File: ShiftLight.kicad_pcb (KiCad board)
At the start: 2 copper layers, 63 x 12 mm, 11 parts, among them U1 MSPM0C1104SDDFR, U2 LMR544xx, U3 KTD2052A/B

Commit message: Layout: Import, start placement
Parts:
- added C1: 100n, Capacitor_SMD:C_0805_2012Metric, F.Cu at (109.1, 112.6)
- added C10: 100n, Capacitor_SMD:C_0402_1005Metric, F.Cu at (162.9, 89.8)
- added C11: 10u, Capacitor_SMD:C_1206_3216Metric, F.Cu at (97.6, 110.9)
- added C12: 100n, Capacitor_SMD:C_0402_1005Metric, F.Cu at (162.9, 87.3)
- added C13: 100n, Capacitor_SMD:C_0402_1005Metric, F.Cu at (162.9, 92.3)
- added C2: 100n, Capacitor_SMD:C_0805_2012Metric, F.Cu at (109.1, 109.5)
- added C3: 10n, Capacitor_SMD:C_0402_1005Metric, F.Cu at (94.7, 88.7)
- added C4: 10n, Capacitor_SMD:C_0402_1005Metric, F.Cu at (92.9, 88.1)
- added C5: 100n, Capacitor_SMD:C_0603_1608Metric, F.Cu at (188.9, 79.3)
- added C6: 4.7u, Capacitor_SMD:C_1206_3216Metric, F.Cu at (108.4, 100.3)
- added C7: 100n, Capacitor_SMD:C_0603_1608Metric, F.Cu at (188.9, 81.8)
- added C8: 100n, Capacitor_SMD:C_0402_1005Metric, F.Cu at (137.4, 105.3)
- added C9: 10u, Capacitor_SMD:C_1206_3216Metric, F.Cu at (114.8, 108.9)
- added D10: XLMDK12D, LED_THT:LED_D5.0mm_IRGrey, F.Cu at (133.6, 83.8)
- added D11: XLMDK12D, LED_THT:LED_D5.0mm_IRGrey, F.Cu at (126.3, 83.8)
- added D12: ESDA5V3SC5, Package_TO_SOT_SMD:SOT-23-5, F.Cu at (127.5, 89.2)
- added D9: XLMYK12D, LED_THT:LED_D5.0mm_IRGrey, F.Cu at (119.0, 83.8)
- added F1: F0603G0R15FNTR, Fuse:Fuse_0603_1608Metric, F.Cu at (97.6, 88.1)
- added FB1: BLM15PX601SZ1D, Inductor_SMD:L_0402_1005Metric, F.Cu at (137.4, 103.3)
- added J1: 0533980471, Connector_Molex:Molex_PicoBlade_53398-0471_1x04-1MP_P1.25mm_Vertical, B.Cu at (94.7, 87.3)
- added J2: 0533980571, Connector_Molex:Molex_PicoBlade_53398-0571_1x05-1MP_P1.25mm_Vertical, B.Cu at (126.7, 87.3)
- added JP1: ~, Jumper:SolderJumper-2_P1.3mm_Bridged_RoundedPad1.0x1.5mm, F.Cu at (104.7, 113.4)
- added L1: 15u, Inductor_SMD:L_TDK_VLS3015CX, F.Cu at (112.9, 114.3)
- added R1: 5k6, Resistor_SMD:R_0402_1005Metric, F.Cu at (117.0, 99.9)
- added R10: 68R, Resistor_SMD:R_0402_1005Metric, F.Cu at (96.1, 97.9)
- added R11: 68R, Resistor_SMD:R_0402_1005Metric, F.Cu at (96.1, 99.9)
- added R12: 68R, Resistor_SMD:R_0402_1005Metric, F.Cu at (96.1, 101.9)
- added R13: 68R, Resistor_SMD:R_0402_1005Metric, F.Cu at (99.0, 97.9)
- added R14: 68R, Resistor_SMD:R_0402_1005Metric, F.Cu at (99.0, 99.9)
- added R15: 68R, Resistor_SMD:R_0402_1005Metric, F.Cu at (99.0, 101.9)
- added R2: 1k8, Resistor_SMD:R_0402_1005Metric, F.Cu at (93.0, 89.5)
- added R3: 100k, Resistor_SMD:R_0402_1005Metric, F.Cu at (188.9, 84.4)
- added R4: 32k, Resistor_SMD:R_0402_1005Metric, F.Cu at (188.9, 86.9)
- added R5: 3k3, Resistor_SMD:R_0402_1005Metric, F.Cu at (162.9, 94.9)
- added R6: 3k3, Resistor_SMD:R_0402_1005Metric, F.Cu at (162.9, 97.4)
- added R7: 68R, Resistor_SMD:R_0402_1005Metric, F.Cu at (93.2, 99.9)
- added R8: 68R, Resistor_SMD:R_0402_1005Metric, F.Cu at (93.2, 101.9)
- added R9: 5k6, Resistor_SMD:R_0402_1005Metric, F.Cu at (93.2, 97.9)
- added TP1: ~, TestPoint:TestPoint_Pad_D1.0mm, F.Cu at (119.1, 108.5)
- added TP2: ~, TestPoint:TestPoint_Pad_D1.0mm, F.Cu at (134.5, 103.9)
- added TP3: ~, TestPoint:TestPoint_Pad_D1.0mm, F.Cu at (134.5, 106.9)
- added TP4: ~, TestPoint:TestPoint_Pad_D1.0mm, F.Cu at (119.1, 105.4)
- added TP5: ~, TestPoint:TestPoint_Pad_D1.0mm, F.Cu at (72.9, 74.9)
- added TP6: ~, TestPoint:TestPoint_Pad_D1.0mm, F.Cu at (93.3, 110.8)
- added U4: TLC59208F, Package_DFN_QFN:Texas_RGY_R-PVQFN-N16_EP2.05x2.55mm_ThermalVias, B.Cu at (109.0, 87.9)
- added U5: VEML7700, Sensor:Vishay_VEML7700, F.Cu at (90.0, 78.6)
- added U6: TLV803E, Package_TO_SOT_SMD:SOT-323_SC-70, F.Cu at (94.0, 117.4)
- D1: value LD271 -> PMEG6010ER; footprint LED_THT:LED_D5.0mm_IRGrey -> Diode_SMD:Nexperia_CFP3_SOD-123W; moved to B.Cu
- D2: value LD271 -> SMAJ30CA; footprint LED_THT:LED_D5.0mm_IRGrey -> Diode_SMD:D_SMA
- D3: value LD271 -> VESD05B1-02V; footprint LED_THT:LED_D5.0mm_IRGrey -> Diode_SMD:D_SOD-523
- D4, D5, D6: value LD271 -> XLVG12D
- D7, D8: value LD271 -> XLMYK12D
- U1: value MSPM0C1104SDDFR -> VOS618A; footprint Package_TO_SOT_SMD:SOT-23-8 -> Package_SO:SSOP-4_4.4x2.6mm_P1.27mm
- U2: value LMR544xx -> LMR51406YDBV
- U3: value KTD2052A/B -> MSPM0C1104SDDFR; footprint Package_DFN_QFN:DFN-8-1EP_2x2mm_P0.5mm_EP0.9x1.5mm -> Package_TO_SOT_SMD:SOT-23-8
- moved U1 60.5 mm to (85.9, 88.9), turned to 180 degrees
- moved D4 40.7 mm to (82.5, 83.8)
- moved U3 34.8 mm to (167.4, 93.1)
- moved D6 34.4 mm to (97.1, 83.8), turned to 0 degrees
- moved D8 27.6 mm to (111.7, 83.8), turned to 0 degrees
- moved D2 18.0 mm to (102.8, 89.2), turned to 180 degrees
- moved D1 16.6 mm to (102.1, 84.7), turned to -90 degrees
- moved D5 13.2 mm to (89.8, 83.8)
- moved D3 12.1 mm to (90.9, 88.8)
- moved U2 11.7 mm to (150.1, 79.5)
- moved D7 8.47 mm to (104.4, 83.8)
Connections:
- net 12V0 renamed Net-(JP1-B)
- D1 pad 1: unconnected-(D1-K-Pad1) -> 12V_IN
- D1 pad 2: unconnected-(D1-A-Pad2) -> Net-(D1-A)
- D2 pad 1: unconnected-(D2-K-Pad1) -> GND
- D2 pad 2: unconnected-(D2-A-Pad2) -> Net-(D1-A)
- D3 pad 1: unconnected-(D3-K-Pad1) -> Net-(D3-K)
- D3 pad 2: unconnected-(D3-A-Pad2) -> Net-(D3-A)
- D4 pad 1: unconnected-(D4-K-Pad1) -> Net-(D4-K)
- D4 pad 2: unconnected-(D4-A-Pad2) -> Net-(D4-A)
- D5 pad 1: unconnected-(D5-K-Pad1) -> Net-(D5-K)
- D5 pad 2: unconnected-(D5-A-Pad2) -> Net-(D5-A)
- D6 pad 1: unconnected-(D6-K-Pad1) -> Net-(D6-K)
- D6 pad 2: unconnected-(D6-A-Pad2) -> Net-(D6-A)
- D7 pad 1: unconnected-(D7-K-Pad1) -> Net-(D7-K)
- D7 pad 2: unconnected-(D7-A-Pad2) -> Net-(D7-A)
- D8 pad 1: unconnected-(D8-K-Pad1) -> Net-(D8-K)
- D8 pad 2: unconnected-(D8-A-Pad2) -> Net-(D8-A)
- U1 pad 1: unconnected-(U1-PA27/A0-Pad1) -> Net-(D3-K)
- U1 pad 2: unconnected-(U1-PA1/NRST-Pad2) -> Net-(D3-A)
- U1 pad 4: 3V3 -> /01_Input/TACHO
- U3 pad 1: unconnected-(U3-SCL-Pad1) -> /01_Input/TACHO
- U3 pad 2: unconnected-(U3-SDA-Pad2) -> /02_MCU/I2C_SCL
- U3 pad 3: unconnected-(U3-LED4-Pad3) -> GND
- U3 pad 4: unconnected-(U3-LED3-Pad4) -> 3V3
- U3 pad 5: unconnected-(U3-LED2-Pad5) -> /02_MCU/I2C_SDA
- U3 pad 6: unconnected-(U3-LED1-Pad6) -> /02_MCU/SWDIO
- U3 pad 7: GND -> /02_MCU/SWCLK
- U3 pad 8: 3V3 -> Net-(U3-PA24/A3)
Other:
- board size 63 x 12 mm -> 66.3 x 15.2 mm

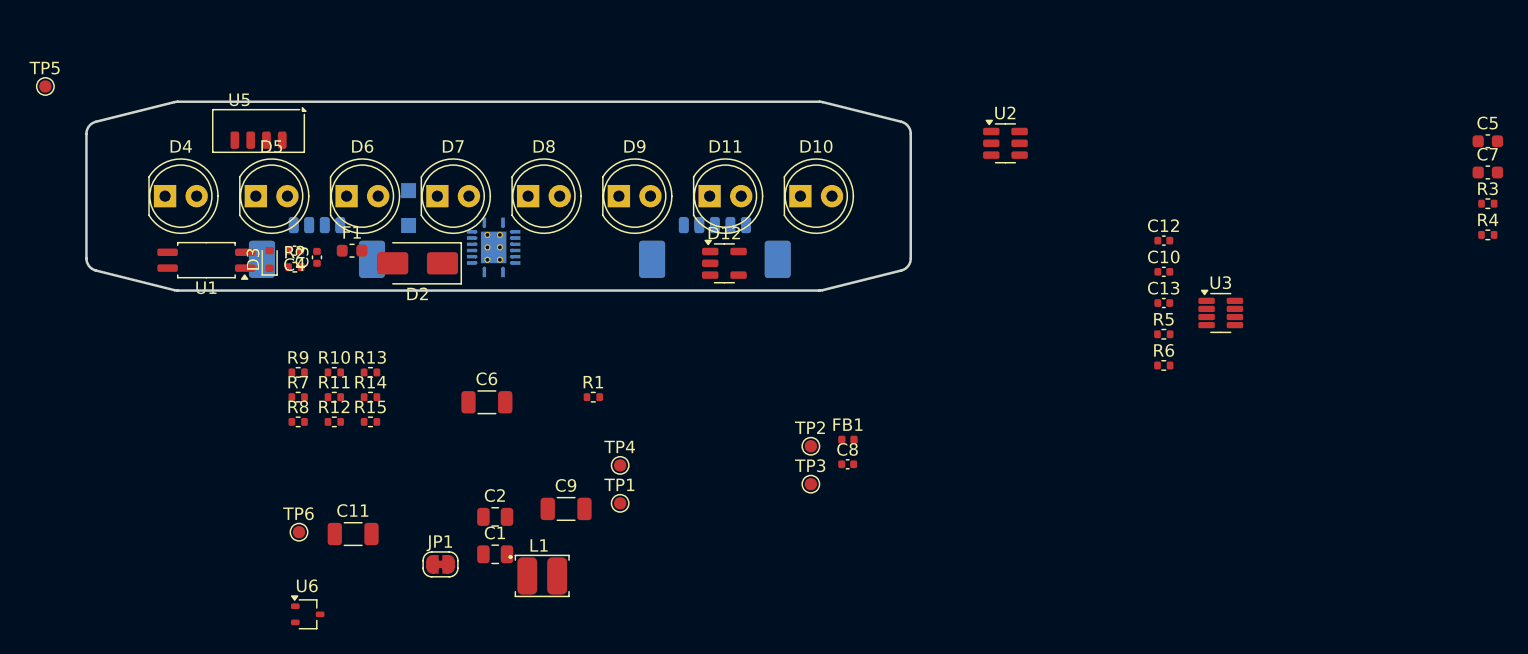
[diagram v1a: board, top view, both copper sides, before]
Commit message: Layout: Initial component placement
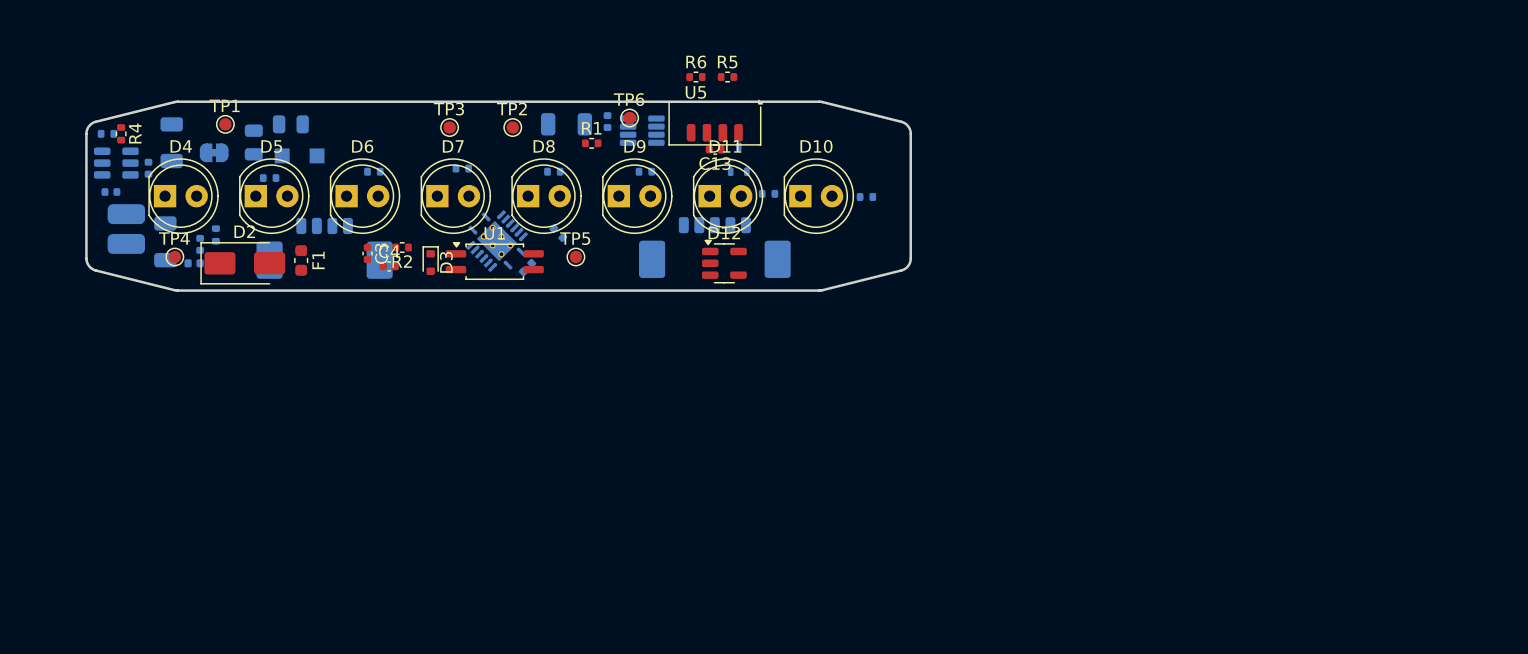
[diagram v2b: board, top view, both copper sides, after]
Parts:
- C1, C10, C11, C12, C2, C6, C8, C9, FB1, JP1, L1, R10, R11, R12, R13, R14, R15, R3, R7, R8, R9, U2, U3, U6: moved to B.Cu
- C5, C7: footprint Capacitor_SMD:C_0603_1608Metric -> Capacitor_SMD:C_0402_1005Metric; moved to B.Cu
- moved R3 111.2 mm to (77.9, 78.7), turned to 180 degrees
- moved C5 110.8 mm to (78.2, 83.4)
- moved R4 110.2 mm to (79.0, 78.7), turned to -90 degrees
- moved C7 107.7 mm to (81.2, 81.5), turned to -90 degrees
- moved U2 71.5 mm to (78.6, 81.1)
- moved C8 55.0 mm to (85.3, 87.6), turned to 90 degrees
- moved FB1 54.5 mm to (84.9, 89.2)
- moved C10 51.2 mm to (111.7, 89.5), turned to -135 degrees
- moved U6 50.4 mm to (128.7, 80.8), turned to 90 degrees
- moved U3 48.8 mm to (120.9, 78.5)
- moved C12 45.8 mm to (118.1, 77.8), turned to -90 degrees
- moved TP5 44.8 mm to (115.6, 88.6)
- moved R6 44.2 mm to (125.2, 74.2)
- moved TP1 44.0 mm to (87.4, 78.0)
- moved L1 43.6 mm to (79.4, 86.4), turned to -90 degrees
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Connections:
- C3 pad 1: Net-(J1-Pin_3) -> Net-(J1-Pin_1)
- D12 pad 1: +3V3 -> /02_MCU/SWDIO
- D12 pad 3: /02_MCU/I2C_SCL -> /02_MCU/SWCLK
- D12 pad 4: /02_MCU/SWDIO -> +3V3
- D12 pad 5: /02_MCU/SWCLK -> /02_MCU/I2C_SCL
- F1 pad 1: Net-(J1-Pin_1) -> Net-(J1-Pin_4)
- J1 pad 2: GND -> Net-(D3-A)
- J1 pad 3: Net-(J1-Pin_3) -> GND
- J1 pad 4: Net-(D3-A) -> Net-(J1-Pin_4)
- R2 pad 2: Net-(J1-Pin_3) -> Net-(J1-Pin_1)

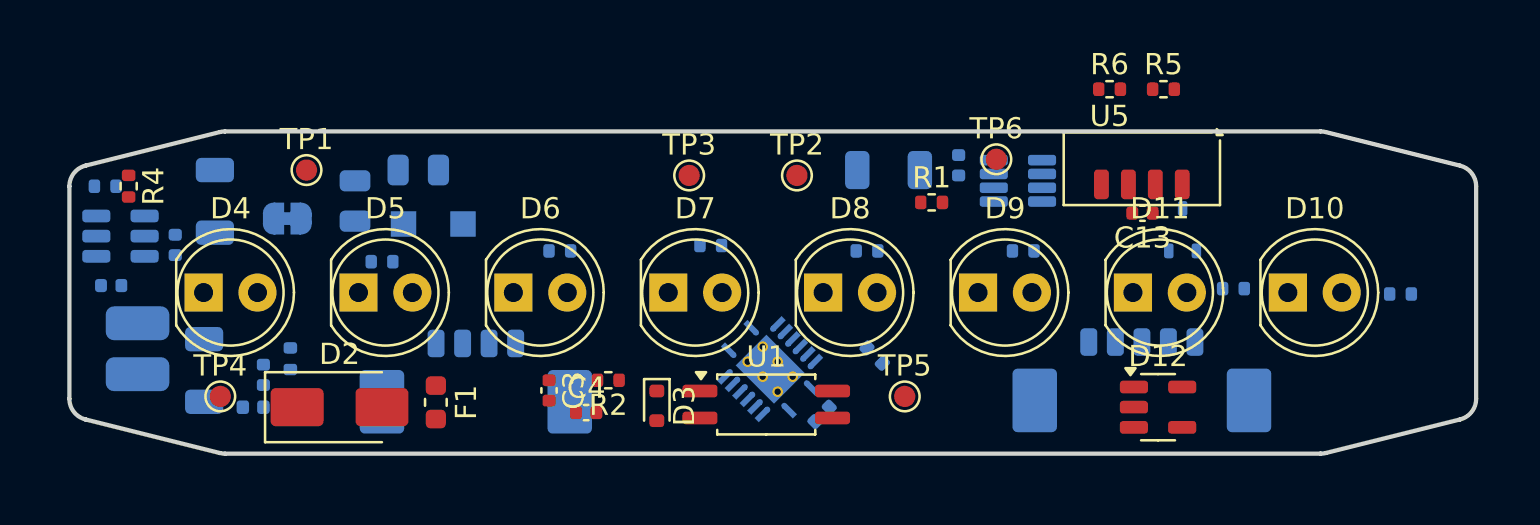
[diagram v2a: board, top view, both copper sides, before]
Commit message: Layout: Finish routing, start silkscreen cleanup
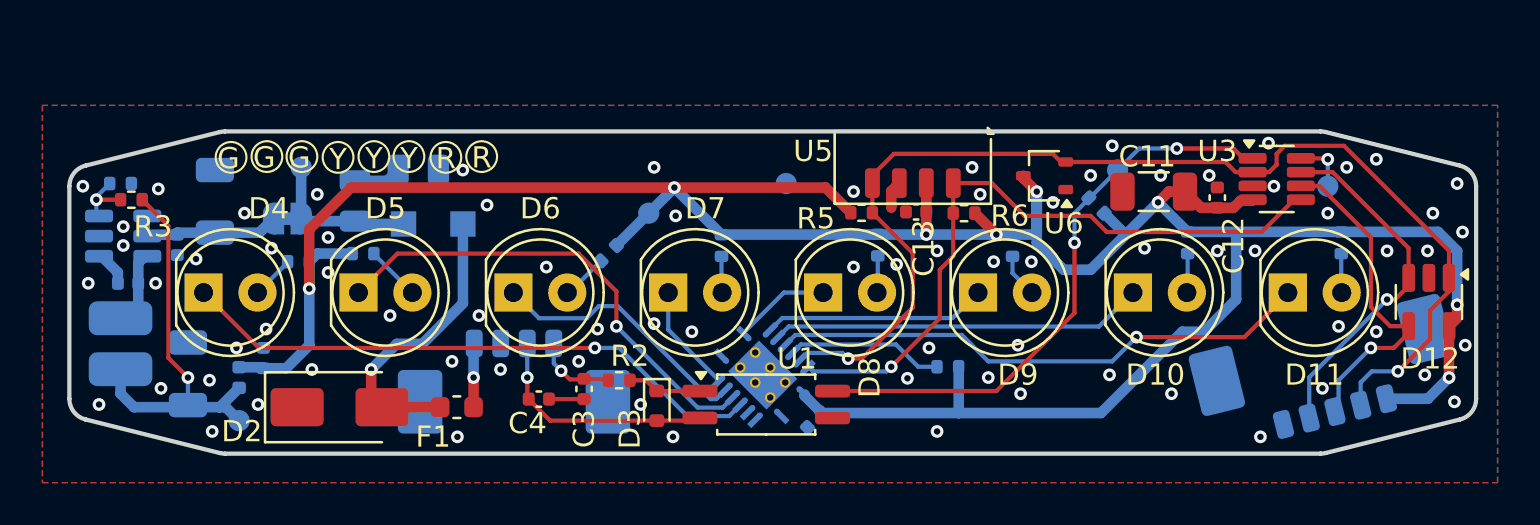
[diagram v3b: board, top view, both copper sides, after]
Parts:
- C11, C12, R3, U3, U6: moved to F.Cu
- R1, R4, TP1, TP2, TP3, TP4, TP5, TP6: moved to B.Cu
- moved TP6 15.7 mm to (135.5, 78.7), turned to 180 degrees
- moved R5 15.4 mm to (113.5, 80.0)
- moved TP5 14.6 mm to (125.6, 78.0), turned to 180 degrees
- moved D12 13.7 mm to (140.3, 84.2), turned to -90 degrees
- moved C11 12.5 mm to (127.3, 79.0)
- moved C12 12.3 mm to (130.3, 79.3), turned to 90 degrees
- moved U3 12.2 mm to (133.1, 78.4)
- moved U5 10.8 mm to (116.0, 77.9)
- moved C13 10.7 mm to (116.1, 79.9)
- moved R14 10.3 mm to (128.9, 81.4), turned to 90 degrees
- moved R6 9.01 mm to (118.4, 80.0), turned to 180 degrees
- moved J2 8.84 mm to (135.5, 88.1), turned to 14 degrees
- moved R1 7.77 mm to (124.6, 79.6), turned to 135 degrees
- moved D10 7.30 mm to (126.3, 83.8)
- moved D11 7.30 mm to (133.6, 83.8)
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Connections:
- D12 pad 1: /02_MCU/SWDIO -> /02_MCU/I2C_SCL
- D12 pad 4: +3V3 -> /02_MCU/SWDIO
- D12 pad 5: /02_MCU/I2C_SCL -> 3V3
- J2 pad 1: +3V3 -> GND
- J2 pad 2: /02_MCU/I2C_SCL -> /02_MCU/SWCLK
- J2 pad 4: /02_MCU/SWCLK -> /02_MCU/I2C_SCL
- J2 pad 5: GND -> 3V3
- U6 pad 3: +3V3 -> 3V3
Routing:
- net 3V3: track 0.00 -> 137.6 mm, vias 0 -> 8
- net /02_MCU/I2C_SCL: track 0.00 -> 53.8 mm, vias 0 -> 2
- net /02_MCU/I2C_SDA: track 0.00 -> 31.9 mm, vias 0 -> 1
- net Net-(D4-K): track 0.00 -> 27.9 mm, vias 0 -> 1
- net /01_Input/TACHO: track 0.00 -> 27.5 mm, vias 0 -> 2
- net Net-(D11-K): track 0.00 -> 25.7 mm, vias 0 -> 1
- net Net-(D5-K): track 0.00 -> 22.5 mm, vias 0 -> 1
- net Net-(C9-Pad2): track 0.00 -> 19.1 mm, vias 0 -> 1
- net Net-(D10-K): track 0.00 -> 17.6 mm
- net /02_MCU/SWCLK: track 0.00 -> 16.7 mm, vias 0 -> 1
- net /02_MCU/SWDIO: track 0.00 -> 15.8 mm, vias 0 -> 1
- net Net-(D1-A): track 0.00 -> 14.1 mm, vias 0 -> 1
- net Net-(D6-K): track 0.00 -> 12.7 mm
- net Net-(D3-A): track 0.00 -> 11.2 mm, vias 0 -> 1
- net Net-(D9-K): track 0.00 -> 10.5 mm
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- added copper zone on B.Cu, net GND
- added copper zone on F.Cu, net GND
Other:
- board text added: "G"
- board text added: "R"
- board text added: "Y"

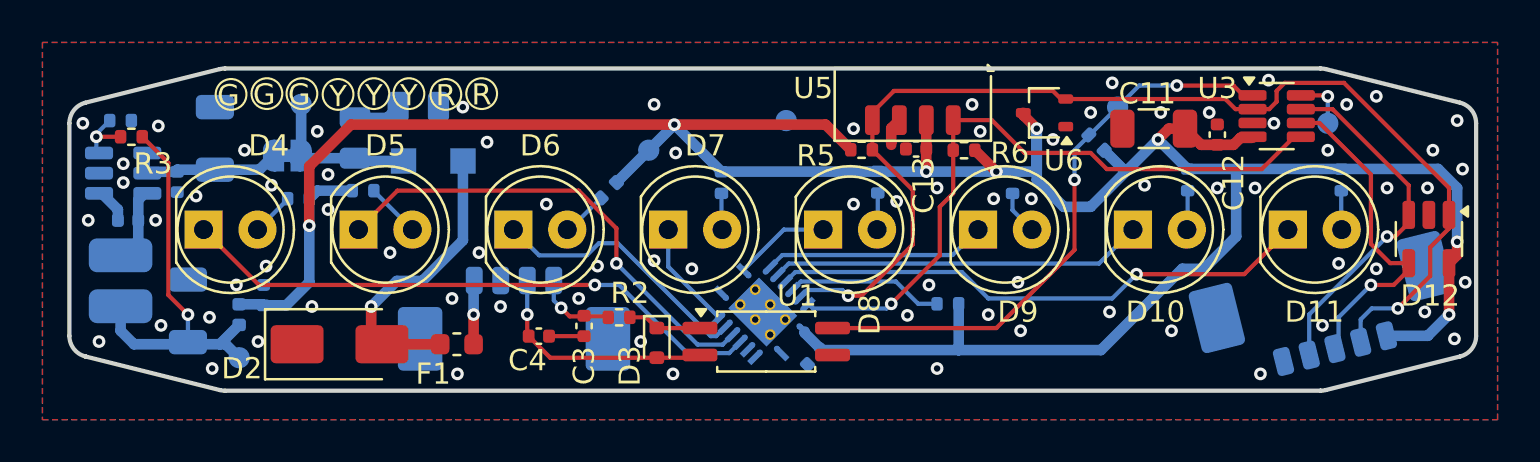
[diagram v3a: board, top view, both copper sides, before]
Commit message: Layout: Cleanup silkscreen and assembly drawing
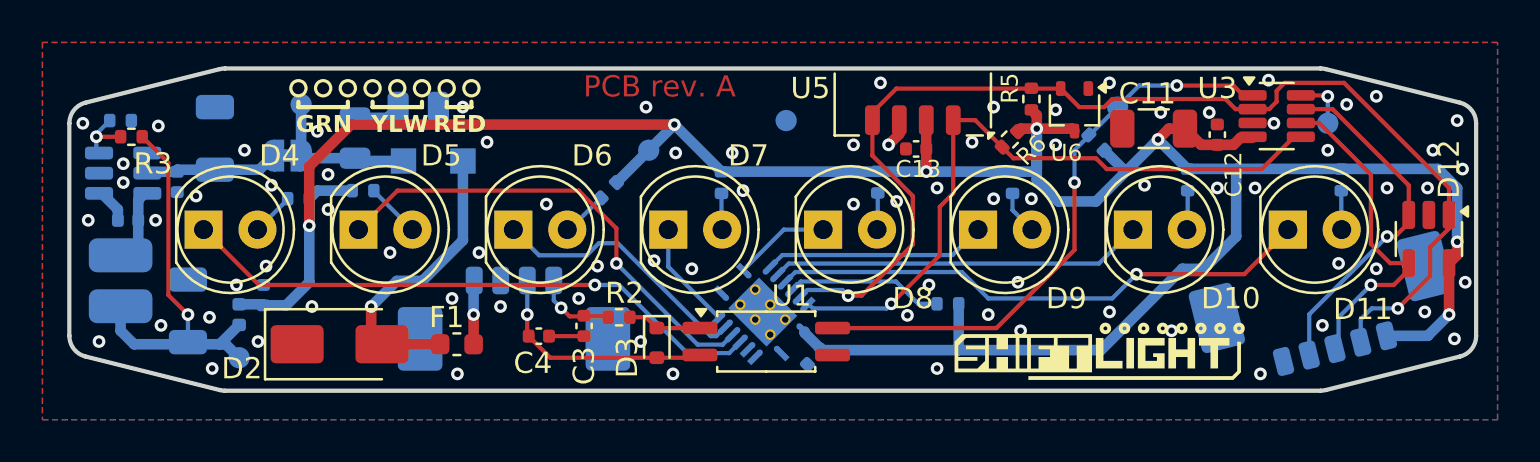
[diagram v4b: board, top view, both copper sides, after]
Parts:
- moved R5 8.35 mm to (121.5, 77.6), turned to 90 degrees
- moved R6 2.22 mm to (120.5, 79.5), turned to -135 degrees
- moved U6 1.42 mm to (123.6, 78.1), turned to -90 degrees
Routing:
- net 3V3: track 137.6 -> 130.0 mm, vias 8 -> 7
- net /02_MCU/I2C_SCL: track 53.8 -> 54.5 mm
- net GND: track 1.32 -> 1.37 mm, vias 77 -> 81
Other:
- board text added: "3V3"
- board text added: "GND"
- board text added: "GRN"
- board text added: "Green"
- board text added: "PCB rev. A"
- board text added: "RED"
- board text added: "Red"
- board text added: "TACHO"
- board text added: "YLW"
- board text added: "Yellow"
- board text removed: "G"
- board text removed: "R"
- board text removed: "Y"
